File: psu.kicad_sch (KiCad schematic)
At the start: 32 parts, among them J6 USB_C_receptacle, U3 TPS628511, U4 TPS628513, U5 MIC5205YM5, U6 MIC5205YM5

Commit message: Add sub-schemes hierarchical labels
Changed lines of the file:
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@@
+    (stroke (width 0) (type default))
+  )
+  (wire (pts (xy 57.785 133.35) (xy 57.785 135.89))
     (stroke (width 0) (type default))
   )
@@
     (stroke (width 0) (type default))
   )
-  (wire (pts (xy 48.895 133.35) (xy 48.895 135.89))
-    (stroke (width 0) (type default))
-  )
   (wire (pts (xy 254 72.39) (xy 243.84 72.39))
     (stroke (width 0) (type default))
@@
     (stroke (width 0) (type default))
   )
-  (wire (pts (xy 60.96 133.35) (xy 60.96 136.525))
+  (wire (pts (xy 47.625 133.35) (xy 47.625 135.89))
     (stroke (width 0) (type default))
   )
@@
     (stroke (width 0) (type default))
   )
-  (global_label "+3V3" (shape input) (at 182.88 53.975 90) (fields_autoplaced)
+  (hierarchical_label "+3V3" (shape output) (at 182.88 53.975 90) (fields_autoplaced)
     (effects (font (size 1.27 1.27)) (justify left))
-    (property "Intersheetrefs" "${INTERSHEET_REFS}" (at 182.88 45.9098 90)
-      (effects (font (size 1.27 1.27)) (justify left) hide)
-    )
-  )
-  (global_label "+4V0" (shape input) (at 182.88 113.03 90) (fields_autoplaced)
+  )
+  (hierarchical_label "+2V8" (shape output) (at 254 52.07 90) (fields_autoplaced)
     (effects (font (size 1.27 1.27)) (justify left))
-    (property "Intersheetrefs" "${INTERSHEET_REFS}" (at 182.88 104.9648 90)
-      (effects (font (size 1.27 1.27)) (justify left) hide)
-    )
-  )
-  (global_label "+1V3" (shape input) (at 254.635 118.11 90) (fields_autoplaced)
+  )
+  (hierarchical_label "+4V0" (shape output) (at 182.88 113.03 90) (fields_autoplaced)
     (effects (font (size 1.27 1.27)) (justify left))
-    (property "Intersheetrefs" "${INTERSHEET_REFS}" (at 254.635 110.0448 90)
-      (effects (font (size 1.27 1.27)) (justify left) hide)
-    )
-  )
-  (global_label "+2V8" (shape input) (at 254 52.07 90) (fields_autoplaced)
+  )
+  (hierarchical_label "+1V3" (shape output) (at 254.635 118.11 90) (fields_autoplaced)
     (effects (font (size 1.27 1.27)) (justify left))
-    (property "Intersheetrefs" "${INTERSHEET_REFS}" (at 254 44.0048 90)
-      (effects (font (size 1.27 1.27)) (justify left) hide)
-    )
-  )
-  (global_label "+3V3" (shape input) (at 48.895 133.35 90) (fields_autoplaced)
-    (effects (font (size 1.27 1.27)) (justify left))
-    (property "Intersheetrefs" "${INTERSHEET_REFS}" (at 48.895 125.2848 90)
-      (effects (font (size 1.27 1.27)) (justify left) hide)
-    )
   )
   (symbol (lib_id "power:GND") (at 104.14 140.97 0) (unit 1)
@@
         (path "/e63e39d7-6ac0-4ffd-8aa3-1841a4541b55/14127be2-0eb7-46a7-b020-4fb807865184"
           (reference "R12") (unit 1)
-        )
-      )
-    )
-  )
-  (symbol (lib_id "power:PWR_FLAG") (at 48.895 135.89 180) (unit 1)
-    (in_bom yes) (on_board yes) (dnp no) (fields_autoplaced)
-    (property "Reference" "#FLG0102" (at 48.895 137.795 0)
-      (effects (font (size 1.27 1.27)) hide)
-    )
-    (property "Value" "PWR_FLAG" (at 48.895 140.97 0)
-      (effects (font (size 1.27 1.27)))
-    )
-    (property "Footprint" "" (at 48.895 135.89 0)
-      (effects (font (size 1.27 1.27)) hide)
-    )
-    (property "Datasheet" "~" (at 48.895 135.89 0)
-      (effects (font (size 1.27 1.27)) hide)
-    )
-    (pin "1")
-    (instances
-      (project "Mobile_Camera"
-        (path "/e63e39d7-6ac0-4ffd-8aa3-1841a4541b55/14127be2-0eb7-46a7-b020-4fb807865184"
-          (reference "#FLG0102") (unit 1)
         )
       )
@@
     )
   )
+  (symbol (lib_id "power:PWR_FLAG") (at 47.625 135.89 180) (unit 1)
+    (in_bom yes) (on_board yes) (dnp no) (fields_autoplaced)
+    (property "Reference" "#FLG02" (at 47.625 137.795 0)
+      (effects (font (size 1.27 1.27)) hide)
+    )
+    (property "Value" "PWR_FLAG" (at 47.625 140.97 0)
+      (effects (font (size 1.27 1.27)))
+    )
+    (property "Footprint" "" (at 47.625 135.89 0)
+      (effects (font (size 1.27 1.27)) hide)
+    )
+    (property "Datasheet" "~" (at 47.625 135.89 0)
+      (effects (font (size 1.27 1.27)) hide)
+    )
+    (pin "1")
+    (instances
+      (project "Mobile_Camera"
+        (path "/e63e39d7-6ac0-4ffd-8aa3-1841a4541b55/14127be2-0eb7-46a7-b020-4fb807865184"
+          (reference "#FLG02") (unit 1)
+        )
+      )
+    )
+  )
   (symbol (lib_id "power:+5V") (at 73.66 52.07 0) (unit 1)
     (in_bom yes) (on_board yes) (dnp no) (fields_autoplaced)
@@
     )
   )
-  (symbol (lib_id "power:PWR_FLAG") (at 60.96 136.525 180) (unit 1)
-    (in_bom yes) (on_board yes) (dnp no) (fields_autoplaced)
-    (property "Reference" "#FLG01" (at 60.96 138.43 0)
-      (effects (font (size 1.27 1.27)) hide)
-    )
-    (property "Value" "PWR_FLAG" (at 60.96 140.97 0)
-      (effects (font (size 1.27 1.27)))
-    )
-    (property "Footprint" "" (at 60.96 136.525 0)
-      (effects (font (size 1.27 1.27)) hide)
-    )
-    (property "Datasheet" "~" (at 60.96 136.525 0)
+  (symbol (lib_id "power:PWR_FLAG") (at 57.785 135.89 180) (unit 1)
+    (in_bom yes) (on_board yes) (dnp no)
+    (property "Reference" "#FLG01" (at 57.785 137.795 0)
+      (effects (font (size 1.27 1.27)) hide)
+    )
+    (property "Value" "PWR_FLAG" (at 57.785 140.97 0)
+      (effects (font (size 1.27 1.27)))
+    )
+    (property "Footprint" "" (at 57.785 135.89 0)
+      (effects (font (size 1.27 1.27)) hide)
+    )
+    (property "Datasheet" "~" (at 57.785 135.89 0)
       (effects (font (size 1.27 1.27)) hide)
     )
@@
     )
   )
-  (symbol (lib_id "power:GND") (at 60.96 133.35 180) (unit 1)
-    (in_bom yes) (on_board yes) (dnp no) (fields_autoplaced)
-    (property "Reference" "#PWR01" (at 60.96 127 0)
-      (effects (font (size 1.27 1.27)) hide)
-    )
-    (property "Value" "GND" (at 60.96 128.905 0)
-      (effects (font (size 1.27 1.27)))
-    )
-    (property "Footprint" "" (at 60.96 133.35 0)
-      (effects (font (size 1.27 1.27)) hide)
-    )
-    (property "Datasheet" "" (at 60.96 133.35 0)
+  (symbol (lib_id "power:GND") (at 57.785 133.35 180) (unit 1)
+    (in_bom yes) (on_board yes) (dnp no)
+    (property "Reference" "#PWR01" (at 57.785 127 0)
+      (effects (font (size 1.27 1.27)) hide)
+    )
+    (property "Value" "GND" (at 57.785 129.54 0)
+      (effects (font (size 1.27 1.27)))
+    )
+    (property "Footprint" "" (at 57.785 133.35 0)
+      (effects (font (size 1.27 1.27)) hide)
+    )
+    (property "Datasheet" "" (at 57.785 133.35 0)
       (effects (font (size 1.27 1.27)) hide)
     )
@@
         (path "/e63e39d7-6ac0-4ffd-8aa3-1841a4541b55/14127be2-0eb7-46a7-b020-4fb807865184"
           (reference "R17") (unit 1)
+        )
+      )
+    )
+  )
+  (symbol (lib_id "power:+3V3") (at 47.625 133.35 0) (unit 1)
+    (in_bom yes) (on_board yes) (dnp no) (fields_autoplaced)
+    (property "Reference" "#PWR04" (at 47.625 137.16 0)
+      (effects (font (size 1.27 1.27)) hide)
+    )
+    (property "Value" "+3V3" (at 47.625 128.905 0)
+      (effects (font (size 1.27 1.27)))
+    )
+    (property "Footprint" "" (at 47.625 133.35 0)
+      (effects (font (size 1.27 1.27)) hide)
+    )
+    (property "Datasheet" "" (at 47.625 133.35 0)
+      (effects (font (size 1.27 1.27)) hide)
+    )
+    (pin "1")
+    (instances
+      (project "Mobile_Camera"
+        (path "/e63e39d7-6ac0-4ffd-8aa3-1841a4541b55/14127be2-0eb7-46a7-b020-4fb807865184"
+          (reference "#PWR04") (unit 1)
         )
       )
@@
   )
   (symbol (lib_id "power:+5V") (at 36.83 133.35 0) (unit 1)
-    (in_bom yes) (on_board yes) (dnp no) (fields_autoplaced)
+    (in_bom yes) (on_board yes) (dnp no)
     (property "Reference" "#PWR0138" (at 36.83 137.16 0)
       (effects (font (size 1.27 1.27)) hide)
     )
-    (property "Value" "+5V" (at 36.83 128.27 0)
-      (effects (font (size 1.27 1.27)))
-    )
+    (property "Value" "+5V" (at 36.83 128.905 0)
+      (effects (font (size 1.27 1.27)))
+    )

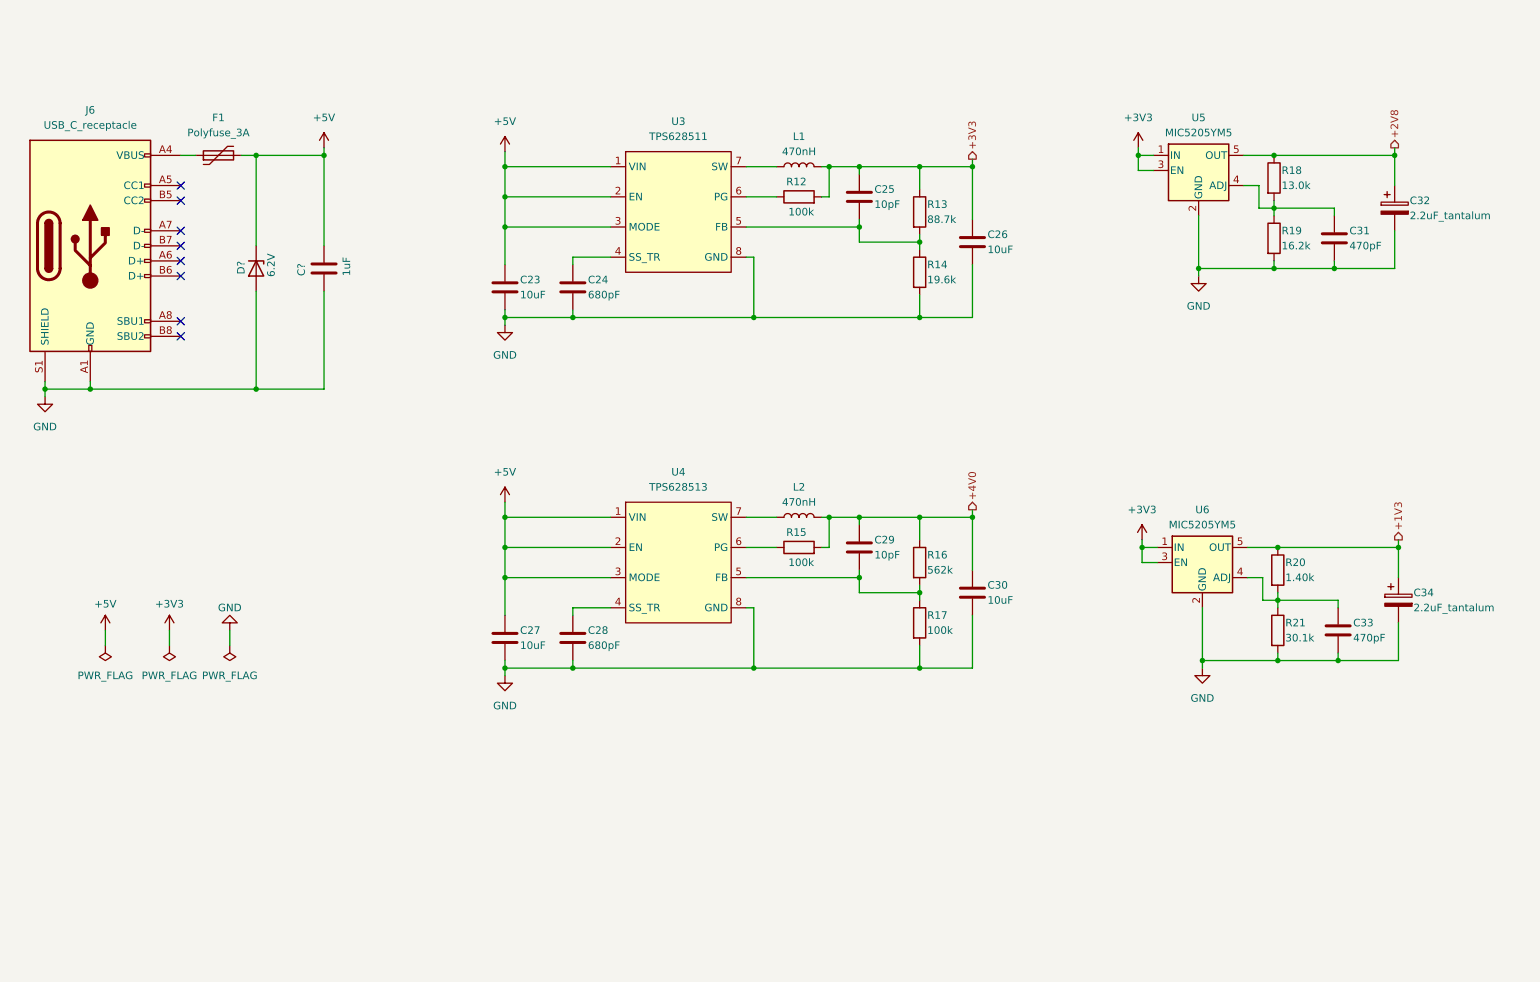
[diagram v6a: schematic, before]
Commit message: Complete the schematic, Begin to layout elements
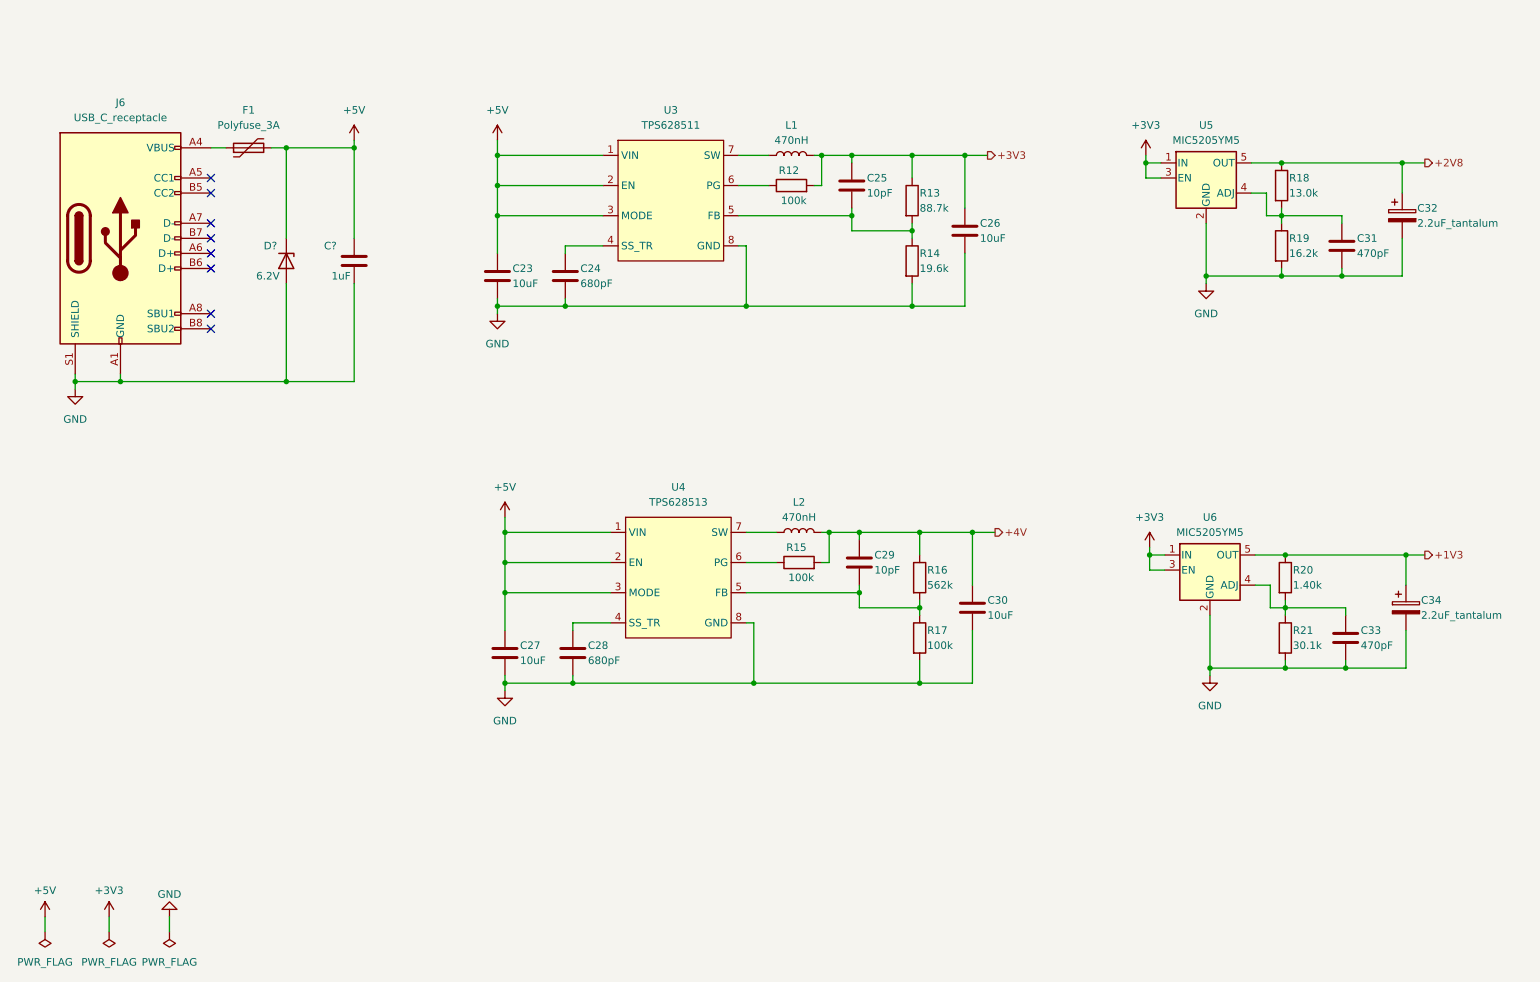
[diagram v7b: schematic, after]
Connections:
- net +4V0 renamed +4V
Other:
- moved on the sheet: C23, C24, C25, C26, C27, C28, C29, C30, C31, C32, C33, C34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
